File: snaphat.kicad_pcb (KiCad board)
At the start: 2 copper layers, 100 x 99.4 mm, 120 parts, among them J1 Conn_01x08_S8B-PH-K-S(LF)(SN), J10 P70-6000045R, J11 P70-6000045R, J12 P70-6000045R, J2 Conn_02x20_2214SM-40G-75-PCR, J3 Conn_01x02_B2B-PH-K-S(LF)(SN), J4 USB_C_USB4930-00-A, J5 Conn_01x03_MC34747, J6 Conn_01x04_SFV4R-3STBE1HLF/C, J7 Conn_01x04_SFV4R-3STBE1HLF/C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

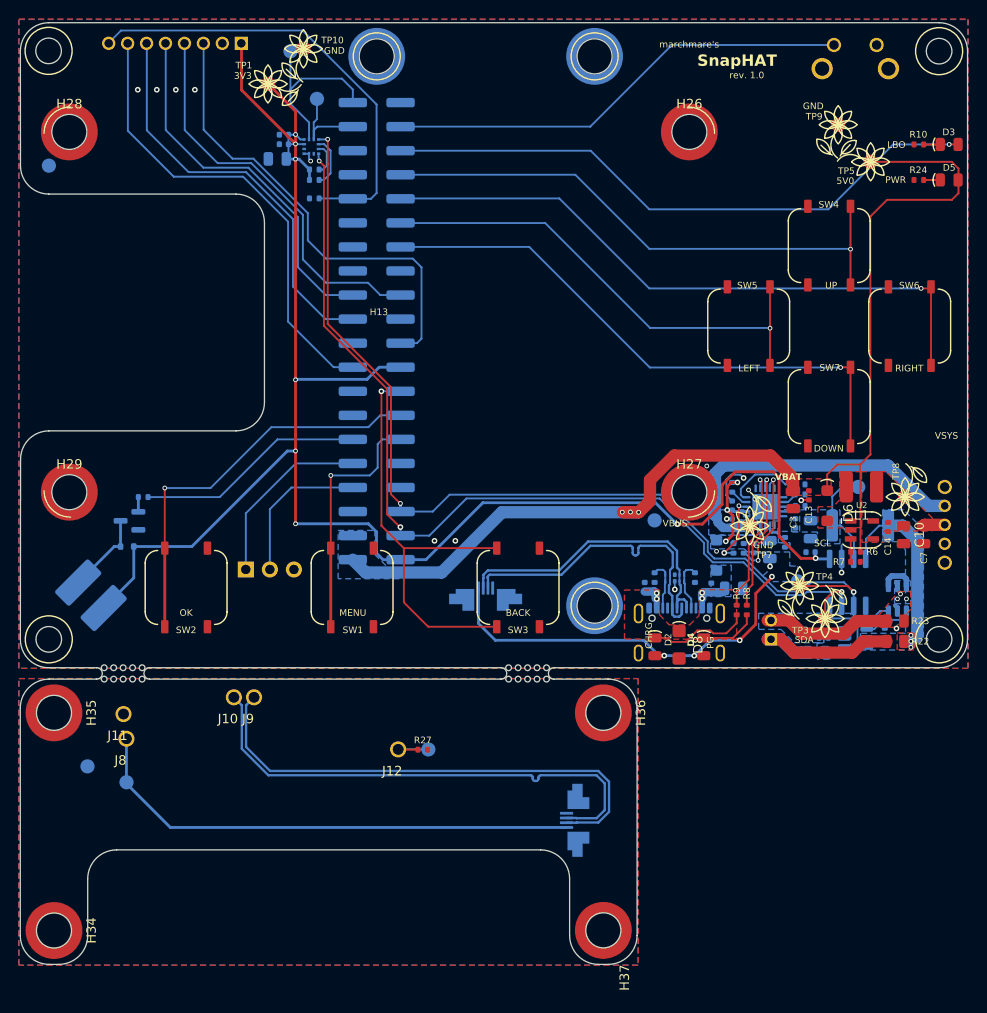
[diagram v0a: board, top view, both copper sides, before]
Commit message: Arrange designators, clear DRC, cleanups
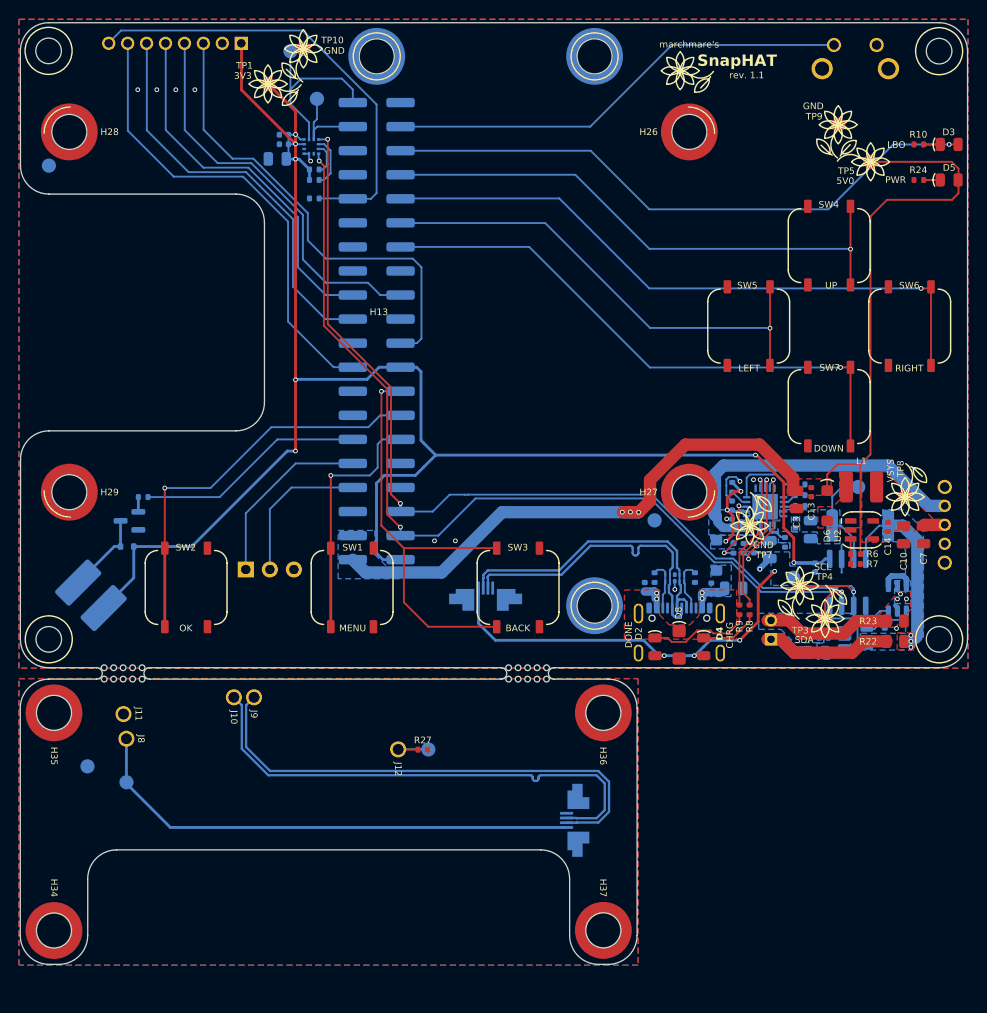
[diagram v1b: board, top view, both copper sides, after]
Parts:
- added REF**: TestPoint_Ornament, library:TestPoint_Ornament, F.Cu at (216.3, 65.5)
- added REF**: TestPoint_Ornament, library:TestPoint_Ornament, B.Cu at (202.2, 134.4)
- moved C1 1.69 mm to (230.6, 117.9), turned to -90 degrees
- moved TP6 0.62 mm to (228.2, 119.0), turned to 90 degrees
- moved C13 0.42 mm to (230.2, 110.0)
- moved C3 0.34 mm to (228.6, 110.7)
- moved R8 0.29 mm to (223.6, 122.4)
- moved R9 0.29 mm to (222.6, 122.4)
- moved R7 0.23 mm to (234.8, 117.5)
- moved R6 0.23 mm to (234.8, 116.5)
- moved R14 0.08 mm to (229.0, 110.3)
- renumbered R3 to R15, R15 to R3
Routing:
- net +5V: track 121.4 -> 122.6 mm
- net /I2C_SCL: track 110.7 -> 109.6 mm
- net /I2C_SDA: track 102.7 -> 101.8 mm
- net VBUS: track 56.4 -> 57.0 mm
- net Net-(U3-~{TE}): track 11.9 -> 11.3 mm
- net GND: track 98.9 -> 98.3 mm, vias 19 -> 13
- net +3.3V: track 185.9 -> 186.4 mm, vias 8 -> 7
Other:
- board text added: "DONE"
- board text added: "OTG"
- board text added: "USB HAT"
- board text added: "rev. ${REVISION}"
- board text removed: "PG"
- board text removed: "rev. 1.0"

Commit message: Add FFC cable info
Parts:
- moved REF** 1.11 mm to (201.8, 133.4), turned to 180 degrees
- moved J7 0.14 mm to (206.7, 144.8)

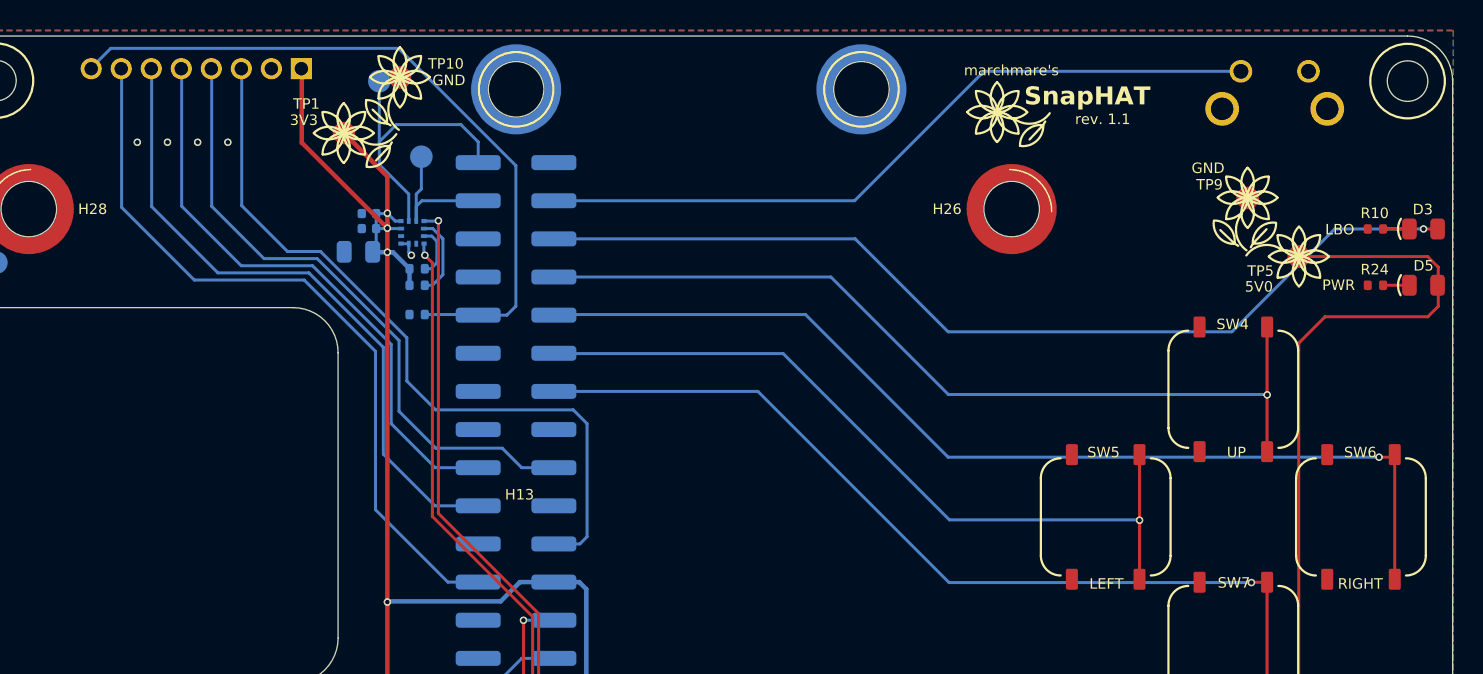
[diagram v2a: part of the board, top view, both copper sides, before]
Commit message: Add LED_SHUTTER
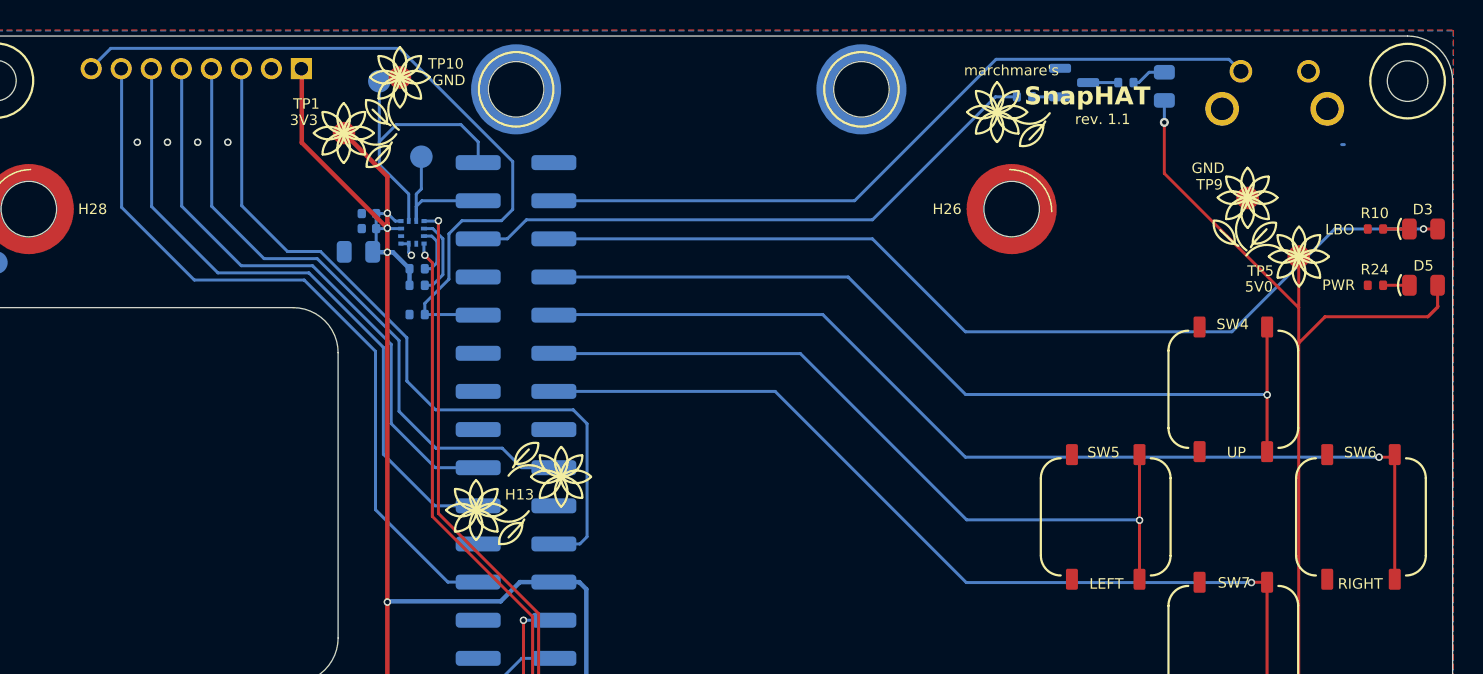
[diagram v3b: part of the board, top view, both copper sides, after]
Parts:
- added D10: 0805 B LED, library:LED_0805_2012Metric, B.Cu at (227.4, 63.8)
- added Q3: Q_BC817-25, library:SOT-23, B.Cu at (221.4, 63.5)
- added R17: 100R, library:R_0402_1005Metric, B.Cu at (224.9, 63.5)
- added R2: 1k, library:R_0402_1005Metric, B.Cu at (218.1, 64.5)
- added REF**: TestPoint_Ornament, library:TestPoint_Ornament, F.Cu at (187.3, 89.8)
- added REF**: TestPoint_Ornament, library:TestPoint_Ornament, F.Cu at (181.6, 92.0)
- added REF**: TestPoint_Ornament, library:TestPoint_Ornament, B.Cu at (227.7, 86.4)
- added REF**: TestPoint_Ornament, library:TestPoint_Ornament, B.Cu at (233.3, 88.6)
- added REF**: TestPoint_Ornament, library:TestPoint_Ornament, B.Cu at (193.0, 91.7)
- added REF**: TestPoint_Ornament, library:TestPoint_Ornament, B.Cu at (198.6, 93.9)
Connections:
- net /LOW_BATTERY renamed /LED_LBO
- net /Power supply/BATTERY_P renamed /Power supply and LEDs/BATTERY_P
- net /Power supply/CHRG_DONE_STAT renamed /Power supply and LEDs/CHRG_DONE_STAT
- net /Power supply/CHRG_STAT renamed /Power supply and LEDs/CHRG_STAT
- net /Power supply/PROG1 renamed /Power supply and LEDs/PROG1
- net /Power supply/PROG2 renamed /Power supply and LEDs/PROG2
- net /Power supply/PROG3 renamed /Power supply and LEDs/PROG3
- net /Power supply/VOUT renamed /Power supply and LEDs/VOUT
- J2 pad 36: unconnected-(J2-Pin_36-Pad36) -> /LED_SHUTTER
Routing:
- net /LED_SHUTTER: track 0.00 -> 39.8 mm
- net +5V: track 122.6 -> 136.1 mm, vias 3 -> 4
- net Net-(D10-K): track 0.00 -> 2.34 mm
- net Net-(Q3-C): track 0.00 -> 2.00 mm
- net Net-(Q3-B): track 0.00 -> 1.85 mm
- net /DISPLAY_BL: track 47.7 -> 49.4 mm
- net /BTN_SHUTTER: track 49.3 -> 50.0 mm

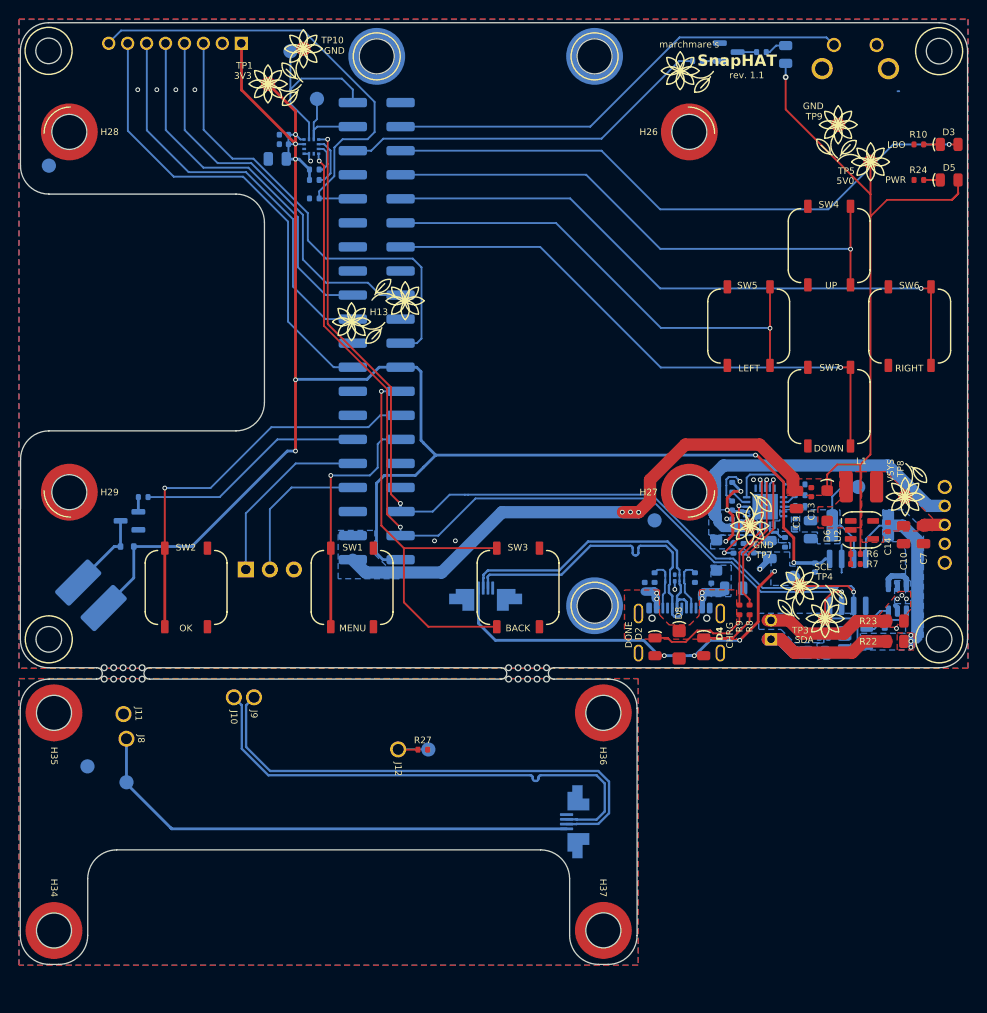
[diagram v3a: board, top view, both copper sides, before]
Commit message: Replace FFC connector with 1mm pitch
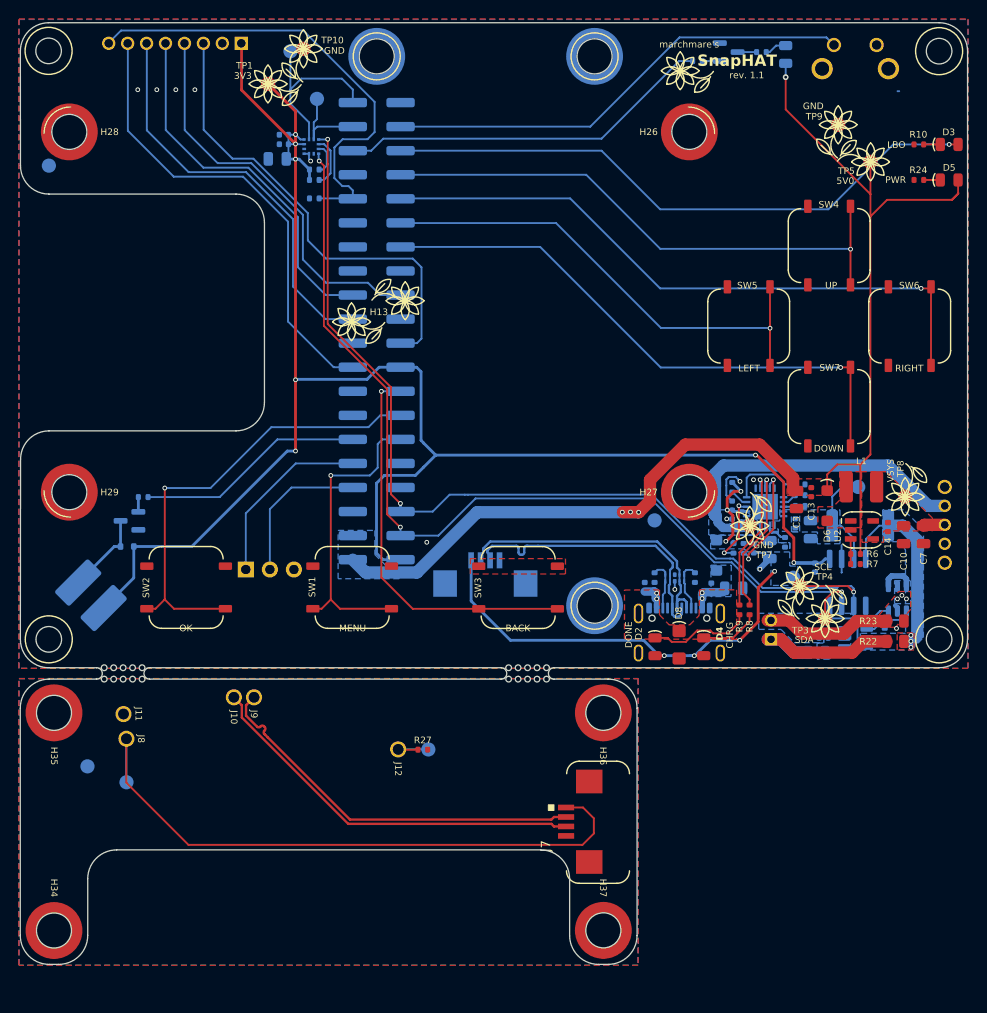
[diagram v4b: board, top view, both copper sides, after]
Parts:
- J6: value Conn_01x04_SFV4R-3STBE1HLF/C -> Conn_01x04_FFC3B11-04-T; footprint library:AMPHENOL_SFV4R-3STBE1HLF -> library:GCT_FFC3B11-04-T
- J7: value Conn_01x04_SFV4R-3STBE1HLF/C -> Conn_01x04_FFC3B11-04-T; footprint library:AMPHENOL_SFV4R-3STBE1HLF -> library:GCT_FFC3B11-04-T; moved to F.Cu
- moved SW3 8.10 mm to (194.3, 117.0), turned to 0 degrees
- moved SW2 8.10 mm to (159.3, 117.0), turned to 0 degrees
- moved SW1 8.10 mm to (176.8, 117.0), turned to 0 degrees
- moved J6 2.88 mm to (195.7, 119.6)
- turned J7 to 90 degrees
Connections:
- J6 pad 1: GND -> VBUS
- J6 pad 2: /USBC_DATA_P -> /USBC_DATA_N
- J6 pad 3: /USBC_DATA_N -> /USBC_DATA_P
- J6 pad 4: VBUS -> GND
- J7 pad 1: /GND_EXT -> /VBUS_EXT
- J7 pad 2: /USBC_EXT_DATA_P -> /USBC_EXT_DATA_N
- J7 pad 3: /USBC_EXT_DATA_N -> /USBC_EXT_DATA_P
- J7 pad 4: /VBUS_EXT -> /GND_EXT
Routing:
- net /VBUS_EXT: track 53.2 -> 66.8 mm
- net /USBC_EXT_DATA_N: track 53.7 -> 41.4 mm
- net /USBC_EXT_DATA_P: track 53.7 -> 41.5 mm
- net /BTN_B: track 46.0 -> 41.6 mm
- net VBUS: track 57.0 -> 59.4 mm
- net /USBC_DATA_P: track 32.6 -> 30.7 mm
- net /USBC_DATA_N: track 32.6 -> 30.8 mm
- net /BTN_A: track 48.1 -> 49.0 mm
- net /BTN_MENU: track 31.8 -> 32.6 mm
- net /DISPLAY_BL: track 49.4 -> 50.0 mm
- net GND: vias 13 -> 12

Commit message: Reroute USB, add shutter LED signal pulldown
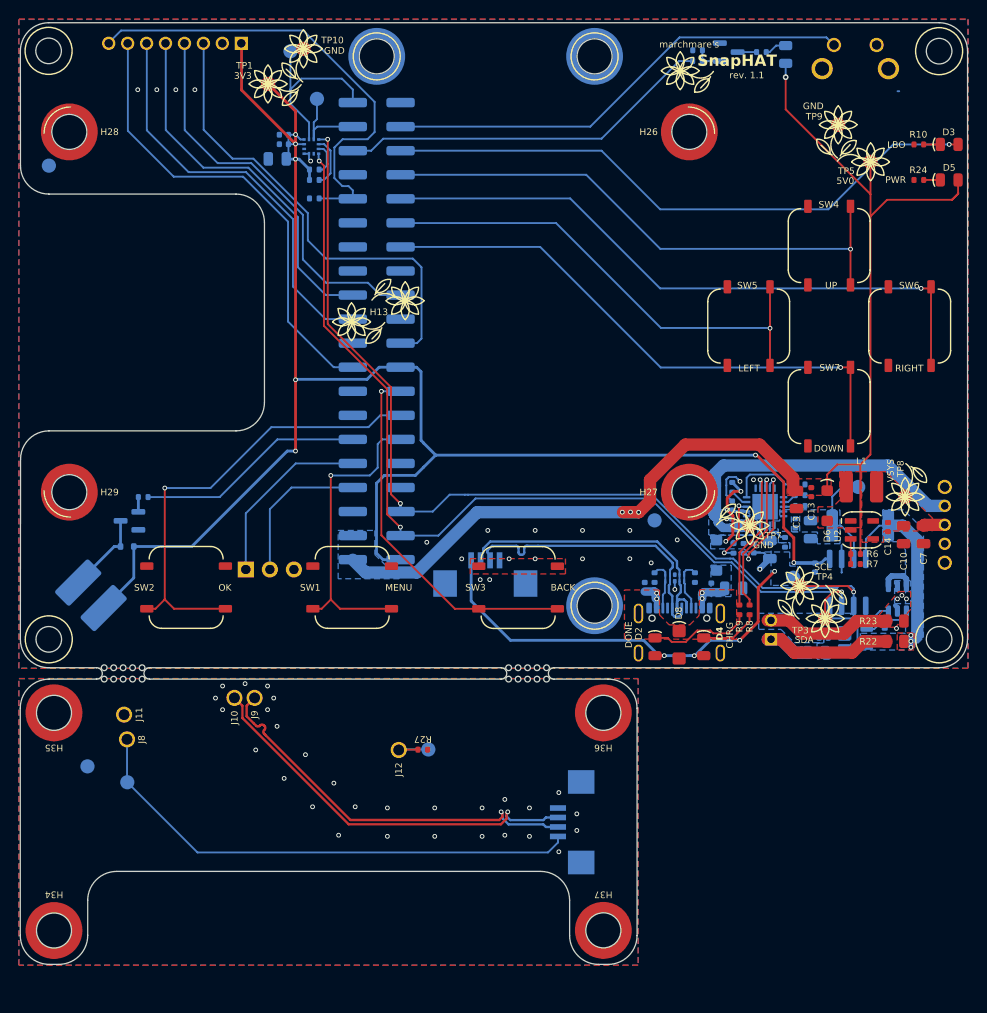
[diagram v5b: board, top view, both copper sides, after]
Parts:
- added R29: 330R, library:R_0402_1005Metric, B.Cu at (218.2, 63.3)
- J7: moved to B.Cu
- moved J7 0.86 mm to (205.9, 144.8), turned to -90 degrees
- moved REF** 0.69 mm to (202.5, 133.4)
- moved J10 0.09 mm to (169.2, 131.7)
- moved J11 0.09 mm to (157.6, 133.4)
- moved J12 0.09 mm to (186.6, 137.2)
- moved J8 0.09 mm to (157.9, 136.1)
- moved J9 0.09 mm to (171.4, 131.7)
- moved TP16 0.09 mm to (157.9, 140.6)
- turned TP7 to -90 degrees
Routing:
- net /VBUS_EXT: track 66.8 -> 54.2 mm
- net /BTN_B: track 41.6 -> 39.0 mm
- net Net-(Q3-B): track 1.85 -> 3.00 mm
- net /USBC_EXT_DATA_N: track 41.4 -> 42.2 mm, vias 0 -> 1
- net /USBC_EXT_DATA_P: track 41.5 -> 42.3 mm, vias 0 -> 1
- net GND: vias 12 -> 25
- net /GND_EXT: vias 0 -> 29
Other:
- outline, holes or cut-outs redrawn
